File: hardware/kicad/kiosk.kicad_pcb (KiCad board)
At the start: 2 copper layers, 178 x 116 mm, 16 parts, among them J10 TerminalBlock_MaiXu_MX126-5.0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, J11 TerminalBlock_MaiXu_MX126-5.0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, J12 PinHeader_1x07_P2.54mm_Vertic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, J13 PinHeader_1x09_P2.54mm_Vertic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, J3 PinSocket_1x14_P2.54mm_Vertic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, J4 PinSocket_1x06_P2.54mm_Vertic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, J5 PinSocket_1x04_P2.54mm_Vertic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, J6 PinSocket_1x06_P2.54mm_Vertic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, J7 PinSocket_1x07_P2.54mm_Vertic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, J9 PinHeader_1x03_P2.54mm_Vertic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, U1 ESP32-S3-CAM

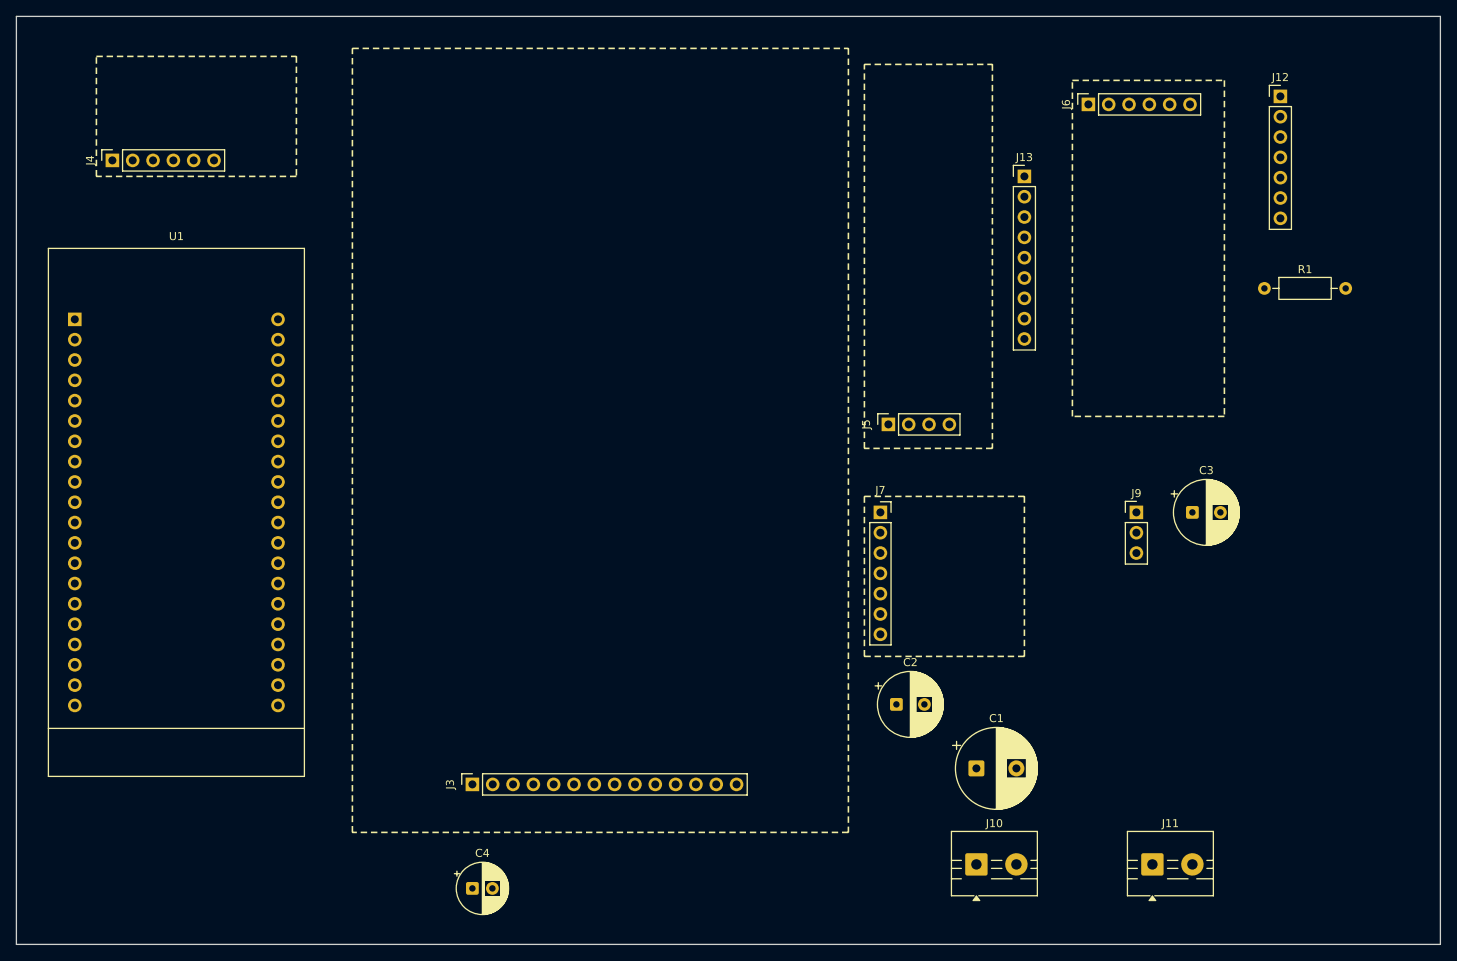
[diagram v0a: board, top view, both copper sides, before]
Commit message: feat(hardware): print every pin name on the silkscreen
A hundred labels, one per pad, so a hole can be identified with the board
in hand instead of the schematic on screen. The board is assembled by
soldering wires into named holes - J13 takes three of them - and an
unlabelled row of nine is a row anyone can miscount.

The devkit's labels go between its two rows, which are 25.4 mm apart and
otherwise empty. Everything else reads outward from its connector.

Ten silkscreen clashes and six labels over copper remain, all between a
label and the outline it sits beside. A smaller font clears them but
falls under the board's minimum text height, which is the worse trade:
silk over a pad is trimmed at fabrication, text too small to read is not.
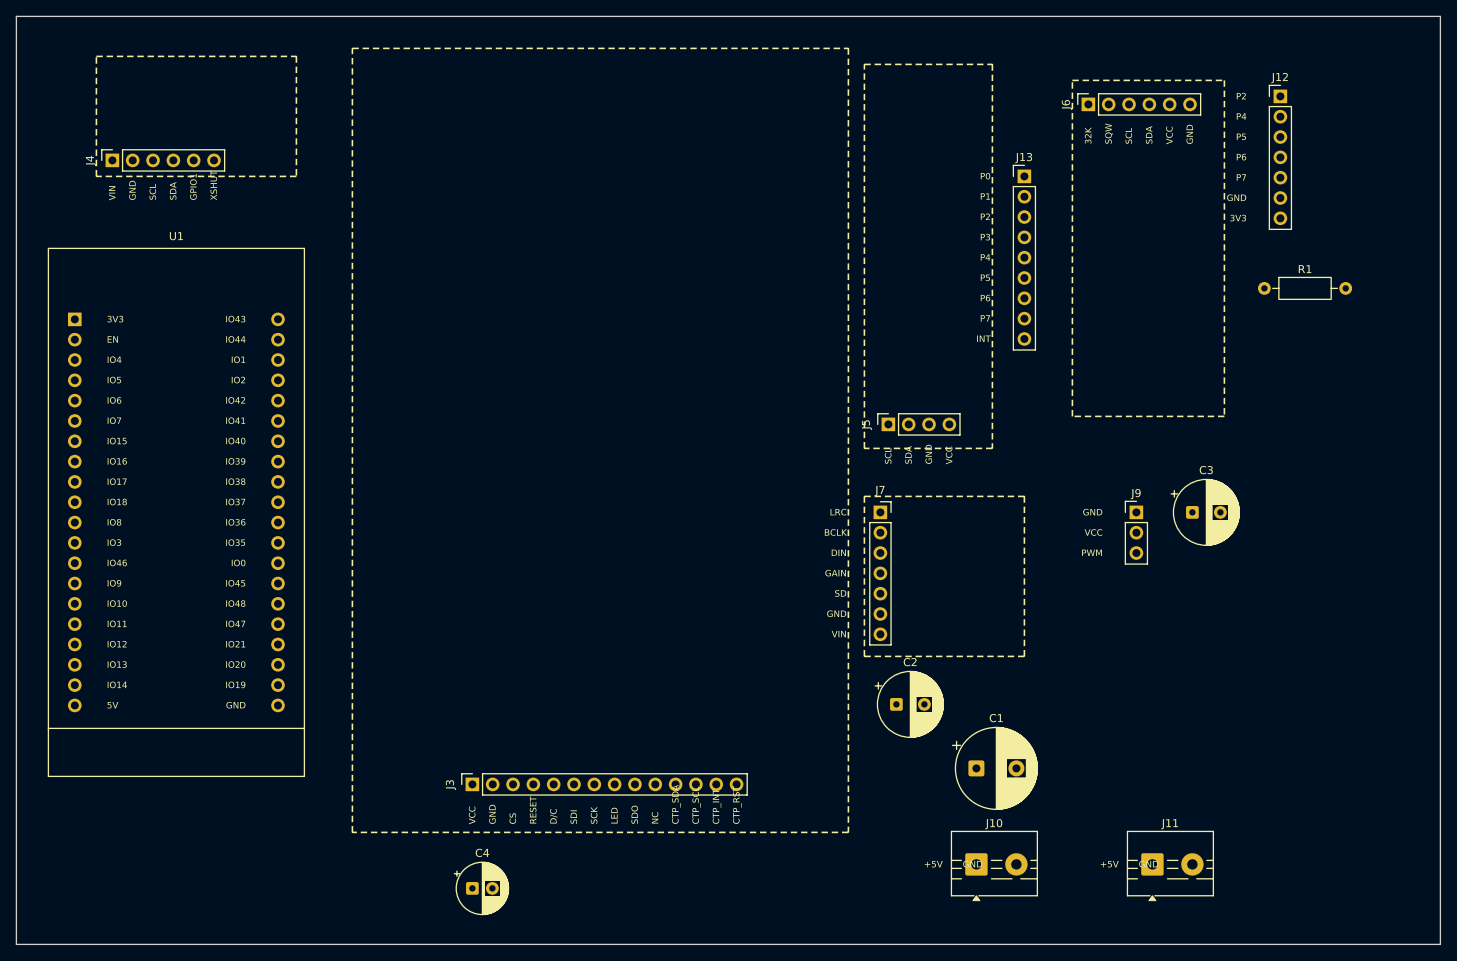
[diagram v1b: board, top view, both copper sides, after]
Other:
- board text added: "+5V"
- board text added: "32K"
- board text added: "3V3"
- board text added: "5V"
- board text added: "BCLK"
- board text added: "CS"
- board text added: "CTP_INT"
- board text added: "CTP_RST"
- board text added: "CTP_SCL"
- board text added: "CTP_SDA"
- board text added: "D/C"
- board text added: "DIN"
- board text added: "EN"
- board text added: "GAIN"
- board text added: "GND"
- board text added: "GPIO1"
- board text added: "INT"
- board text added: "IO0"
- board text added: "IO1"
- board text added: "IO10"
- board text added: "IO11"
- board text added: "IO12"
- board text added: "IO13"
- board text added: "IO14"
- board text added: "IO15"
- board text added: "IO16"
- board text added: "IO17"
- board text added: "IO18"
- board text added: "IO19"
- board text added: "IO2"
- board text added: "IO20"
- board text added: "IO21"
- board text added: "IO3"
- board text added: "IO35"
- board text added: "IO36"
- board text added: "IO37"
- board text added: "IO38"
- board text added: "IO39"
- board text added: "IO4"
- board text added: "IO40"
- board text added: "IO41"
- board text added: "IO42"
- board text added: "IO43"
- board text added: "IO44"
- board text added: "IO45"
- board text added: "IO46"
- board text added: "IO47"
- board text added: "IO48"
- board text added: "IO5"
- board text added: "IO6"
- board text added: "IO7"
- board text added: "IO8"
- board text added: "IO9"
- board text added: "LED"
- board text added: "LRC"
- board text added: "NC"
- board text added: "P0"
- board text added: "P1"
- board text added: "P2"
- board text added: "P3"
- board text added: "P4"
- board text added: "P5"
- board text added: "P6"
- board text added: "P7"
- board text added: "PWM"
- board text added: "RESET"
- board text added: "SCK"
- board text added: "SCL"
- board text added: "SD"
- board text added: "SDA"
- board text added: "SDI"
- board text added: "SDO"
- board text added: "SQW"
- board text added: "VCC"
- board text added: "VIN"
- board text added: "XSHUT"

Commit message: refactor(hardware): drop J12 and the six spare holes it fed
J12 brought the expander's unused port pins out to a header. That made
sense while J13 was a socket underneath the module, where those pins were
buried. It stopped making sense the moment the port row became soldered
wire: a wire can be soldered wherever it is wanted, so a landing pad on
this board buys nothing.

The same argument empties six of J13's nine holes, so J13 becomes the
three the firmware actually drives - P0, P1, P3 - and the SPARE nets go
with it.

Section 2.4 still names the expander as the only room to grow, and now
says where that room is: the module's own port row, which stays exposed,
not a connector on this board.

Fifteen parts, twenty-two nets.
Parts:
- removed J12: PinHeader_1x07_P2.54mm_Vertical, Connector_PinHeader_2.54mm:PinHeader_1x07_P2.54mm_Vertical
- J13: value PinHeader_1x09_P2.54mm_Vertical -> PinHeader_1x03_P2.54mm_Vertical; footprint Connector_PinHeader_2.54mm:PinHeader_1x09_P2.54mm_Vertical -> Connector_PinHeader_2.54mm:PinHeader_1x03_P2.54mm_Vertical
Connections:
- J13 pad 3: SPARE_P2 -> AMP_SD
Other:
- board text removed: "INT"
- board text removed: "P2"
- board text removed: "P4"
- board text removed: "P5"
- board text removed: "P6"
- board text removed: "P7"

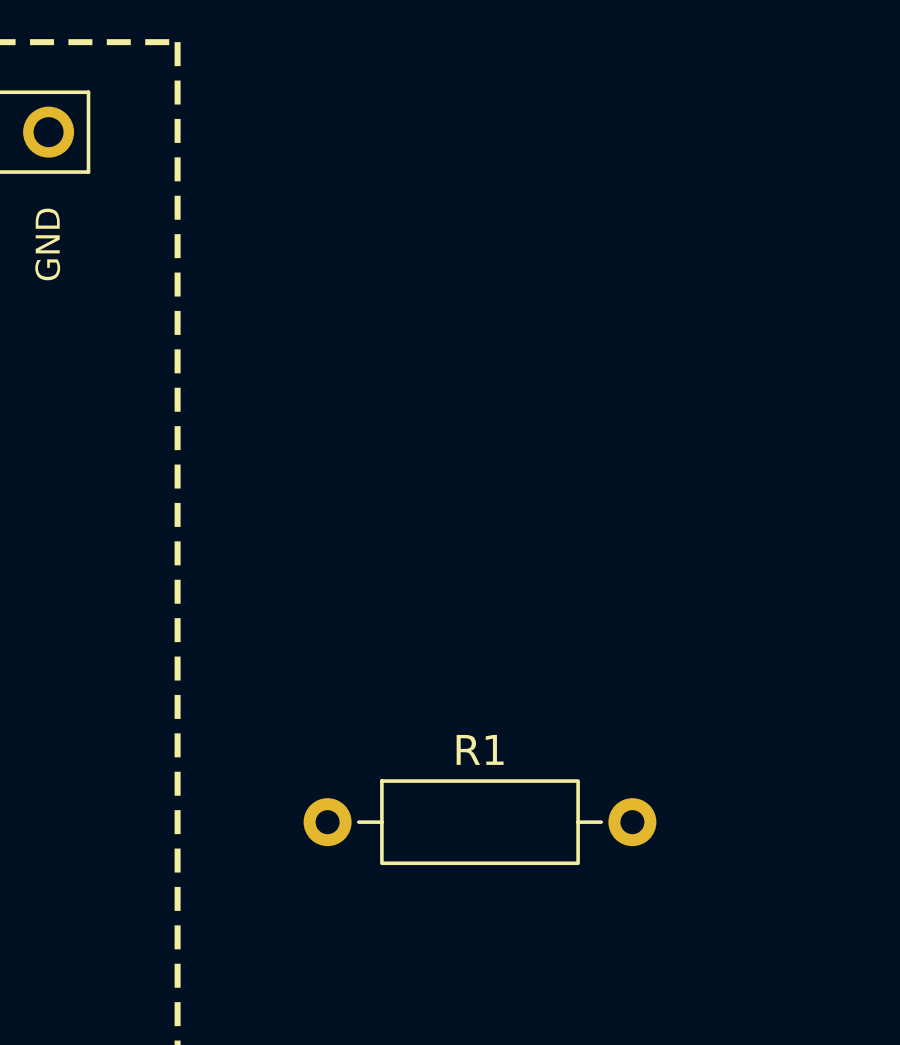
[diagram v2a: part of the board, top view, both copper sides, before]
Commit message: fix(hardware): move the pull-up next to the bus it pulls up
R1 sat alone in the right corner, 26 mm from the nearest I2C pad and as
far again from a 3V3 one, for no reason beyond being where there was
room. Beside the RTC its two legs reach 11 and 23 mm.

At 400 kHz over this board the distance changes nothing electrically -
the bus is one node either way. It changes what the board looks like to
someone tracing it, and a pull-up parked away from its bus reads as an
accident.
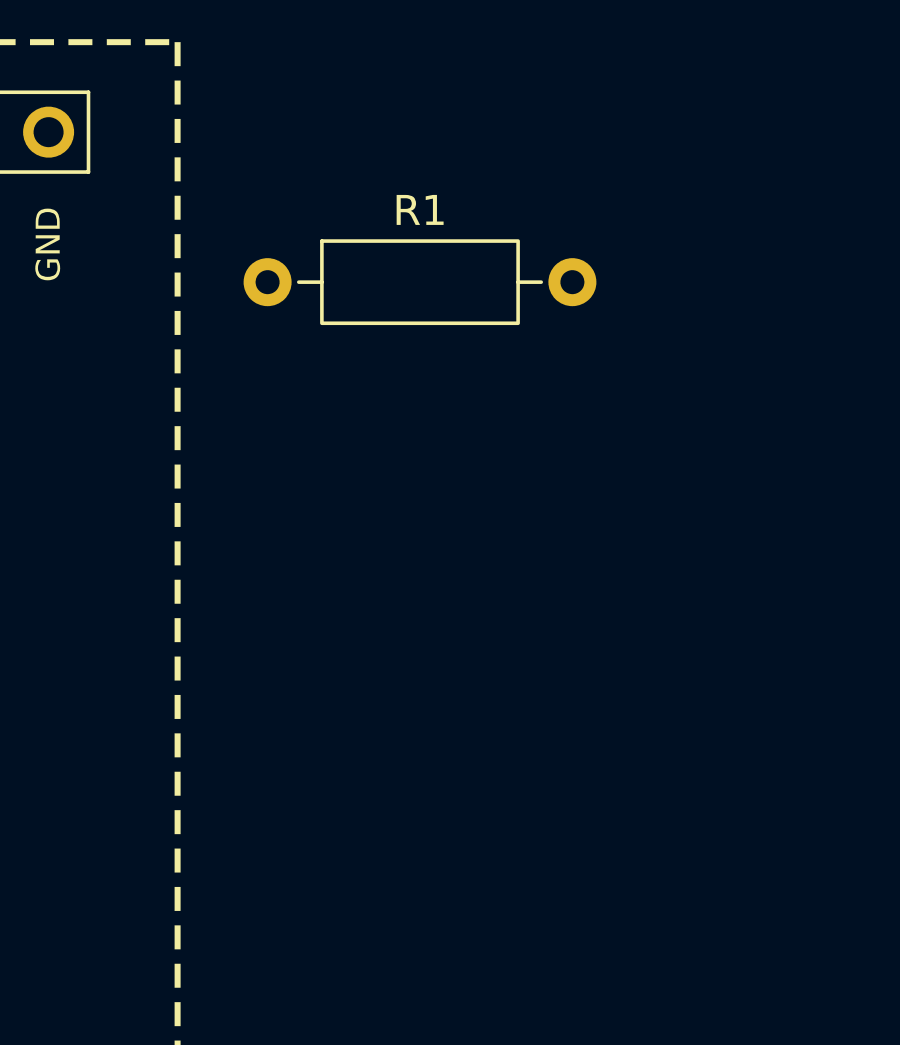
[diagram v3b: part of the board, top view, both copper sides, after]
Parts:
- moved R1 18.1 mm to (154.0, 16.0)
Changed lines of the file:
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@@
 	(footprint "Resistor_THT:R_Axial_DIN0207_L6.3mm_D2.5mm_P10.16mm_Horizontal"
 		(layer "F.Cu")
-		(at 156 34)
+		(at 154 16)
 		(descr "Resistor, Axial_DIN0207 series, Axial, Horizontal, pin pitch=10.16mm, 0.25W = 1/4W, length*diameter=6.3*2.5mm^2, http://cdn-reichelt.de/documents/datenblatt/B400/1_4W%23YAG.pdf")
 		(tags "Resistor Axial_DIN0207 series Axial Horizontal pin pitch 10.16mm 0.25W = 1/4W length 6.3mm diameter 2.5mm")

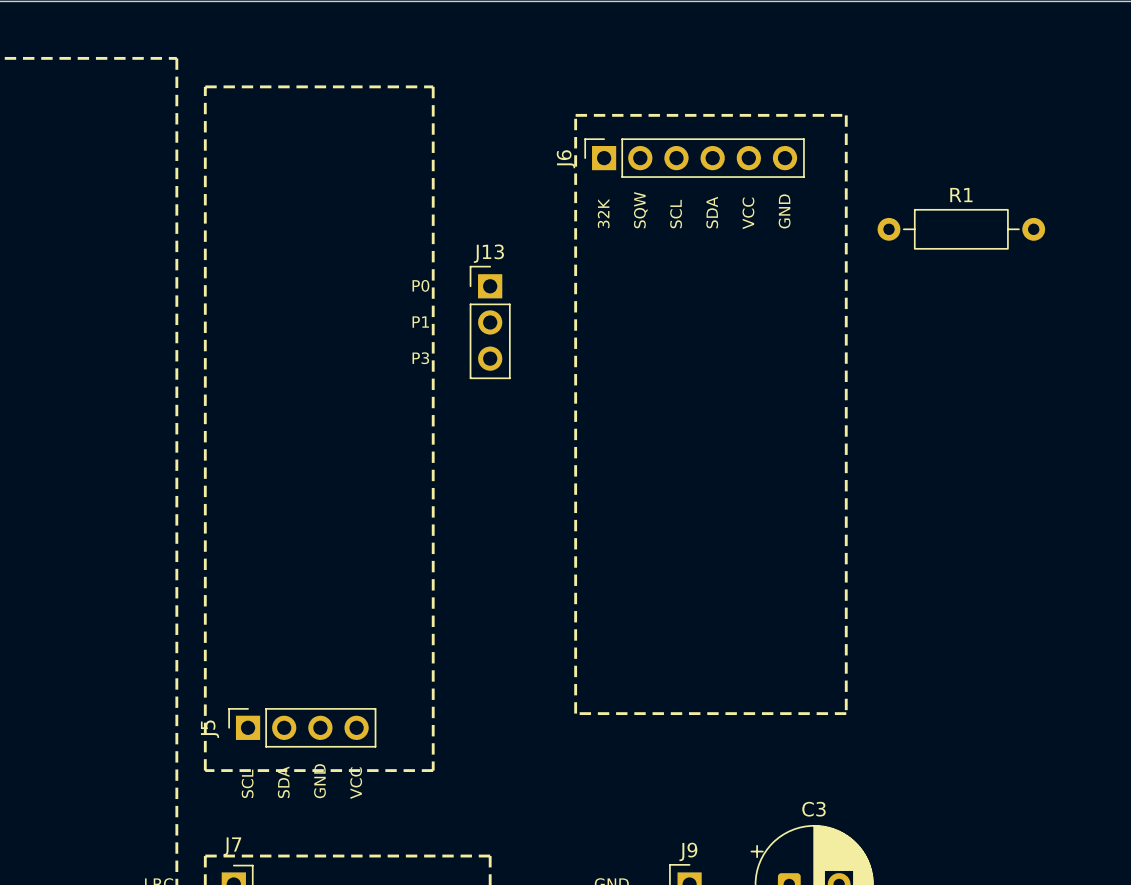
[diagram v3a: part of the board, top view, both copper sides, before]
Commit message: fix(hardware): seat the expander on its port row and free the RTC's area
Three corrections, all from looking at the parts rather than at my model
of them.

The expander seats on the nine-pin row down its long edge, not on the
four-pin row across the short one. Nine pins over 48 mm hold it; four
over 16 mm leave it cantilevered on a board that carries a servo. So J13
becomes the socket and J5 the four holes that take wires from the bus row
standing up above it. The six port pins carrying no signal still need
holes - that is what the module stands on.

The RTC does not lie on the board at all; it plugs in standing. It needed
six holes, not the 19 by 42 mm rectangle reserved for it, and that space
goes back.

Three module outlines left where there were five, and the panel's is
confirmed right.
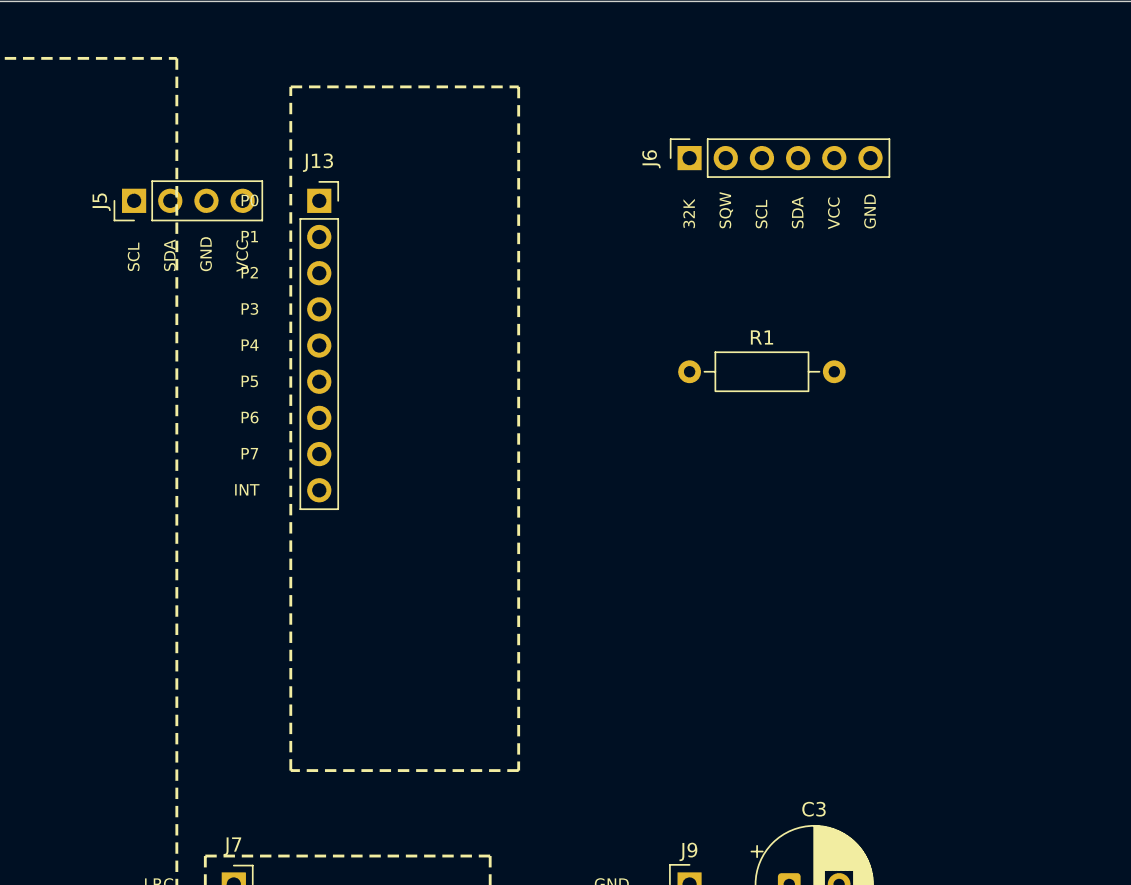
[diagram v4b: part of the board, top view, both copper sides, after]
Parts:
- J13: value PinHeader_1x03_P2.54mm_Vertical -> PinSocket_1x09_P2.54mm_Vertical; footprint Connector_PinHeader_2.54mm:PinHeader_1x03_P2.54mm_Vertical -> Connector_PinSocket_2.54mm:PinSocket_1x09_P2.54mm_Vertical
- J5: value PinSocket_1x04_P2.54mm_Vertical -> PinHeader_1x04_P2.54mm_Vertical; footprint Connector_PinSocket_2.54mm:PinSocket_1x04_P2.54mm_Vertical -> Connector_PinHeader_2.54mm:PinHeader_1x04_P2.54mm_Vertical
- moved J5 37.9 mm to (101.0, 14.0)
- moved R1 17.2 mm to (140.0, 26.0)
- moved J13 13.4 mm to (114.0, 14.0)
- moved J6 6.00 mm to (140.0, 11.0)
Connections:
- J13 pad 3: AMP_SD -> (no net)
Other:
- board text added: "INT"
- board text added: "P2"
- board text added: "P4"
- board text added: "P5"
- board text added: "P6"
- board text added: "P7"
